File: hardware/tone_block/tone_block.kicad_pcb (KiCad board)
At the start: 2 copper layers, 48.1 x 18 mm, 18 parts, among them J1 I/O, Q1 RS32716R

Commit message: Tone block updated from comments
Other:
- board text added: "IN"
- board text added: "OUT"
- board text removed: "In"
- board text removed: "Mix"

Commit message: v1.01
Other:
- board text added: "Tone Block v1.01"

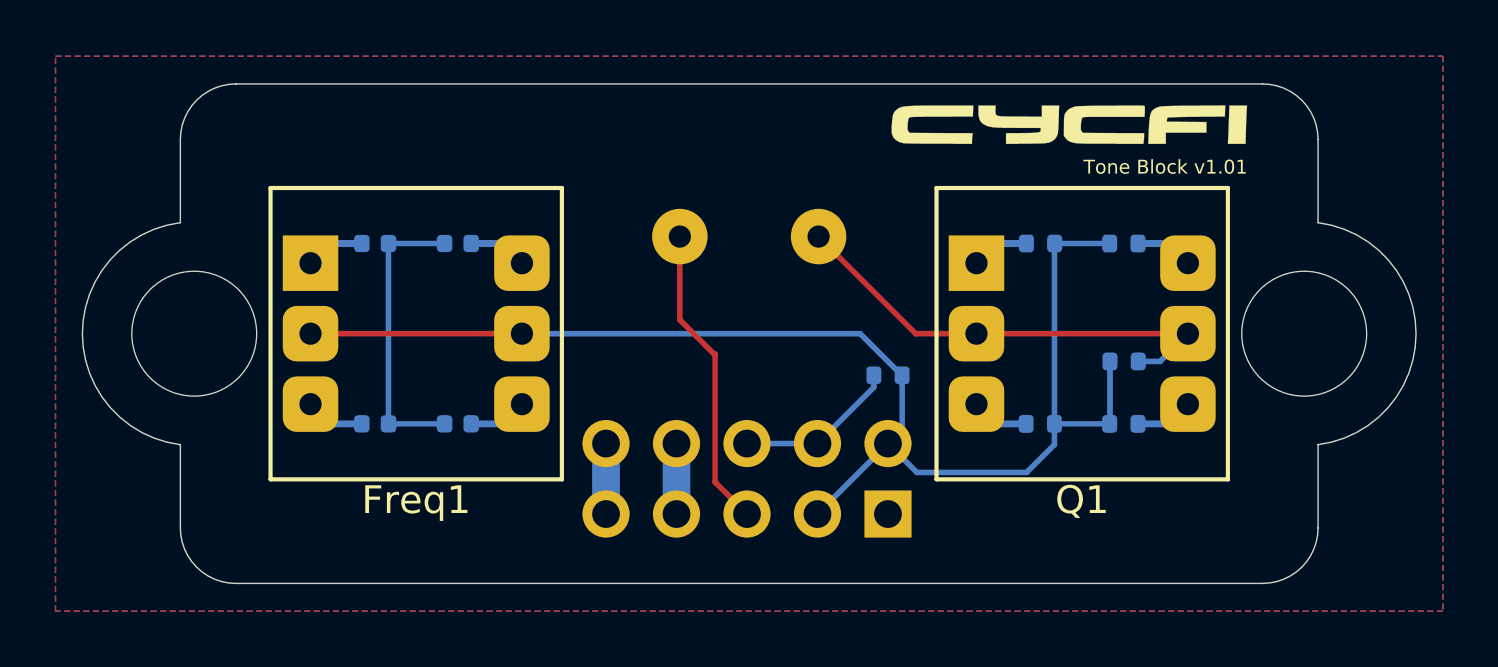
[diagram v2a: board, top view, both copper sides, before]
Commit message: Upgrade to kicad 6
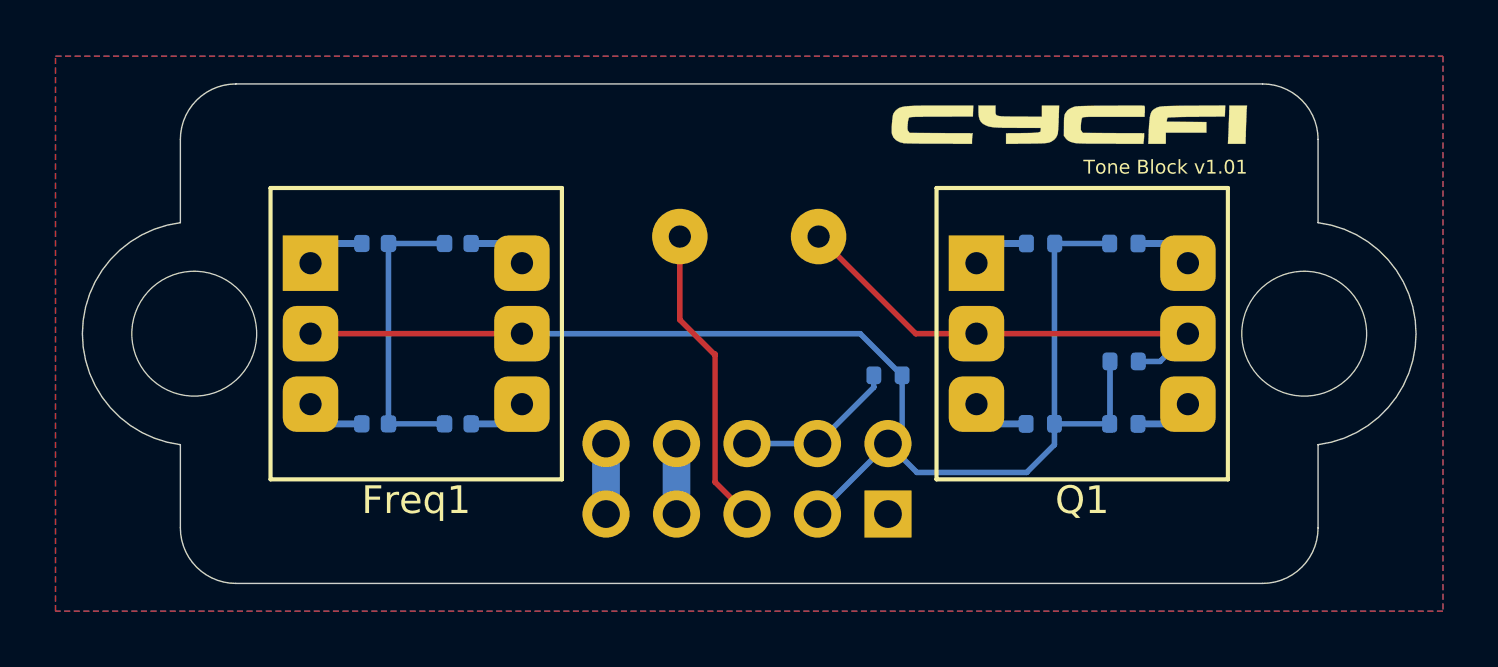
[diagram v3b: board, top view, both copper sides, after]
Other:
- net class Default removed

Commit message: Merge branch 'tone_block_v2' into devel
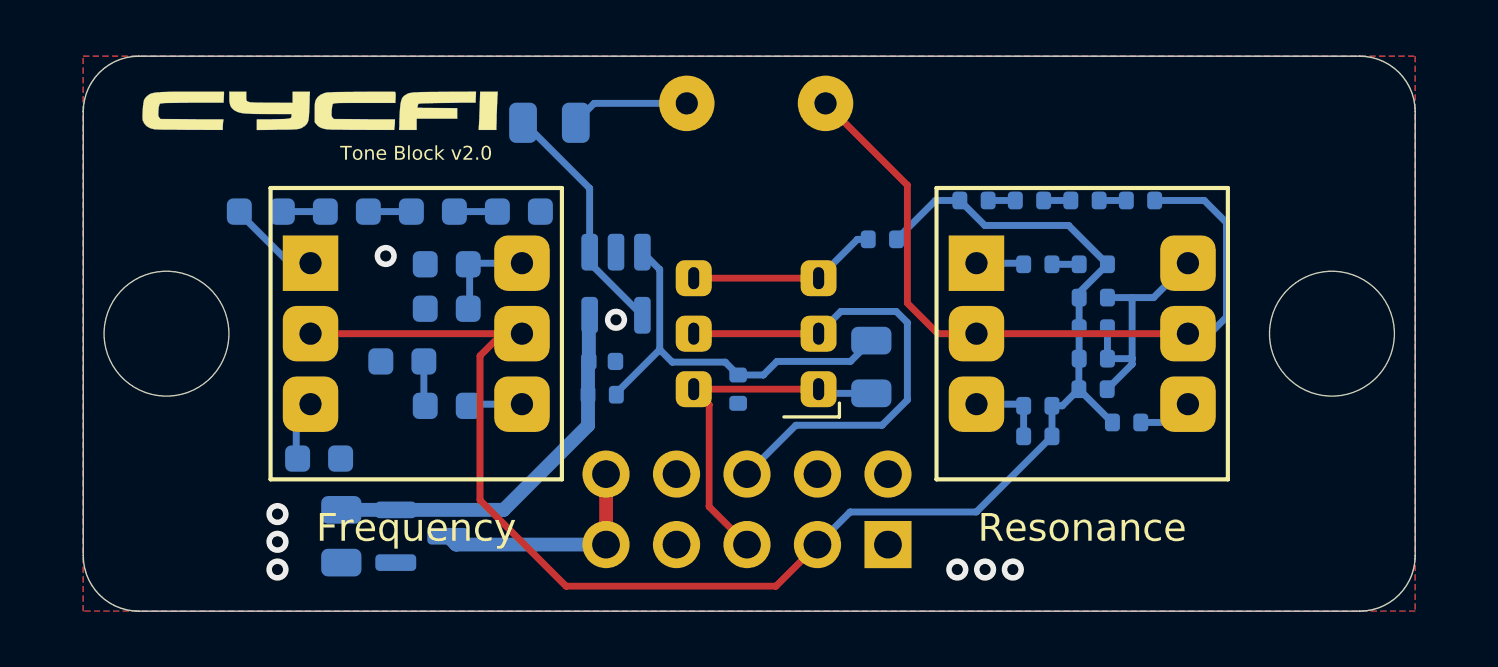
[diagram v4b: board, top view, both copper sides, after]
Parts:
- added C10: 47nF, Capacitor_SMD:C_0603_1608Metric, B.Cu at (190.5, 106.6)
- added C11: 47nF, Capacitor_SMD:C_0603_1608Metric, B.Cu at (192.5, 112.0)
- added C12: 47nF, Capacitor_SMD:C_0603_1608Metric, B.Cu at (193.6, 106.6)
- added C13: 47nF, Capacitor_SMD:C_0603_1608Metric, B.Cu at (196.7, 106.6)
- added C5: 47nF, Capacitor_SMD:C_0603_1608Metric, B.Cu at (187.4, 106.6)
- added C6: 47nF, Capacitor_SMD:C_0603_1608Metric, B.Cu at (194.1, 113.6)
- added C7: 47nF, Capacitor_SMD:C_0603_1608Metric, B.Cu at (189.5, 115.5)
- added C8: 47nF, Capacitor_SMD:C_0603_1608Metric, B.Cu at (194.1, 108.5)
- added C9: 47nF, Capacitor_SMD:C_0603_1608Metric, B.Cu at (194.1, 110.1)
- added Q2: LBSS84LT1G, Package_TO_SOT_SMD:SOT-23, B.Cu at (193.2, 118.3)
- added R10: 330, Resistor_SMD:R_0402_1005Metric, B.Cu at (218.6, 114.2)
- added R11: 330, Resistor_SMD:R_0402_1005Metric, B.Cu at (215.4, 113.6)
- added R12: 330, Resistor_SMD:R_0402_1005Metric, B.Cu at (215.4, 114.7)
- added R13: 330, Resistor_SMD:R_0402_1005Metric, B.Cu at (217.4, 109.7)
- added R14: 330, Resistor_SMD:R_0402_1005Metric, B.Cu at (217.4, 110.8)
- added R15: 330, Resistor_SMD:R_0402_1005Metric, B.Cu at (217.4, 111.9)
- added R16: 330, Resistor_SMD:R_0402_1005Metric, B.Cu at (217.4, 113.0)
- added R7: 330, Resistor_SMD:R_0402_1005Metric, B.Cu at (217.4, 108.5)
- added R8: 4.7k, Resistor_SMD:R_0402_1005Metric, B.Cu at (209.8, 107.6)
- added R9: 330, Resistor_SMD:R_0402_1005Metric, B.Cu at (215.4, 108.5)
- added SW1: DPDT, cycfi_library:PS5801, F.Cu at (207.5, 113.0)
- added U1: TLV170IDBVR, Package_TO_SOT_SMD:SOT-23-5, B.Cu at (200.2, 109.2)
- C1: value 12nF -> 4.7uF; footprint Capacitor_SMD:C_0402_1005Metric -> Capacitor_SMD:C_0805_2012Metric
- C2: value 27nF -> 0.1uF
- C3: value 47nF -> 10uF; footprint Capacitor_SMD:C_0402_1005Metric -> Capacitor_SMD:C_0805_2012Metric
- C4: value 100nF -> 10uF; footprint Capacitor_SMD:C_0402_1005Metric -> Capacitor_SMD:C_0805_2012Metric
- J1: footprint cycfi_library:pin_header_2x05_P2.54mm_vertical -> cycfi_library:pin_header_2x5_P2.54mm_vertical
- R1: value 1.33k -> 100k
- R2: value 665 -> 100k
- R4: value 165 -> 330
- R5: value 82.5 -> 330
- R6: value 4.7k -> 330
- moved G*** 27.5 mm to (220.5, 103.0)
- moved G*** 27.0 mm to (189.5, 103.0)
- moved R1 18.8 mm to (199.7, 113.2)
- moved C3 18.0 mm to (209.4, 112.2), turned to -90 degrees
- moved R2 12.1 mm to (204.6, 113.0), turned to -90 degrees
- moved R6 11.1 mm to (219.1, 106.2), turned to 0 degrees
- moved C1 10.6 mm to (190.3, 118.3), turned to 90 degrees
- moved R3 9.69 mm to (213.1, 106.2)
- moved R4 8.06 mm to (215.1, 106.2), turned to 0 degrees
- moved C2 5.67 mm to (199.7, 112.0), turned to 180 degrees
- moved C4 5.46 mm to (197.8, 103.4), turned to 180 degrees
- moved L1 4.81 mm to (205.2, 102.7)
- moved R5 2.09 mm to (217.1, 106.2)
- moved J1 1.10 mm to (210.0, 118.6)
- moved H1 1.00 mm to (184.0, 111.0)
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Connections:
- C1 pad 1: Net-(C1-Pad1) -> GND
- C1 pad 2: GND -> vcc
- C2 pad 2: Net-(C2-Pad2) -> vcc
- C3 pad 1: GND -> /op+
- C3 pad 2: Net-(C3-Pad2) -> in
- C4 pad 1: GND -> reso_in
- C4 pad 2: Net-(C4-Pad2) -> /op_out
- Freq1 pad 1: Net-(C1-Pad1) -> Net-(C5-Pad1)
- Freq1 pad 2: Net-(C2-Pad2) -> Net-(C6-Pad1)
- Freq1 pad 4: Net-(C3-Pad2) -> Net-(C7-Pad1)
- Freq1 pad 8: Net-(C4-Pad2) -> Net-(C8-Pad1)
- J1 pad 10: ext_cap -> unconnected-(J1-Pad10)
- J1 pad 5: vcc -> v+
- J1 pad 6: vcc -> v+
- J1 pad 8: mix -> out
- J1 pad 9: mix -> unconnected-(J1-Pad9)
- L1 pad 1: in -> reso_in
- R1 pad 1: ext_cap -> vcc
- R1 pad 2: Net-(L1-Pad2) -> /op+
- R2 pad 1: ext_cap -> /op+
- R2 pad 2: Net-(Q1-Pad1) -> GND
- R3 pad 2: Net-(Q1-Pad2) -> Net-(R3-Pad2)
- R4 pad 1: ext_cap -> Net-(R3-Pad2)
- R4 pad 2: Net-(Q1-Pad4) -> Net-(R4-Pad2)
- R5 pad 1: ext_cap -> Net-(R4-Pad2)
- R5 pad 2: Net-(Q1-Pad8) -> Net-(R5-Pad2)
- R6 pad 1: ext_cap -> Net-(R5-Pad2)
- R6 pad 2: mix -> Net-(L1-Pad2)
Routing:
- net out: track 0.00 -> 17.9 mm
- net /op+: track 0.00 -> 14.6 mm
- net GND: track 13.1 -> 0.00 mm, vias 0 -> 8
- net vcc: track 2.54 -> 14.1 mm
- net Net-(L1-Pad2): track 17.5 -> 26.9 mm
- net v+: track 0.00 -> 8.37 mm
- net /op_out: track 0.00 -> 8.32 mm
- net ext_cap: track 48.7 -> 56.9 mm
- net reso_out: track 0.00 -> 6.87 mm
- net Net-(Q1-Pad8): track 2.31 -> 9.08 mm
- net mix: track 5.84 -> 0.00 mm
- net reso_in: track 0.00 -> 4.33 mm
- net Net-(C8-Pad1): track 0.00 -> 3.50 mm
- net Net-(C5-Pad1): track 0.00 -> 3.39 mm
- net Net-(C7-Pad1): track 0.00 -> 2.88 mm
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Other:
- board size 48.1 x 18 mm -> 48 x 20 mm
- board text added: "Frequency"
- board text added: "Resonance"
- board text added: "Tone Block v2.0"
- board text removed: "GND"
- board text removed: "Mix Shunt"
- board text removed: "Tone Block v1.0"
- board text removed: "Tone Block v1.01"
- board text removed: "VCC"

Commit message: Simplified connections (simple IN / OUT, no extra fluff)
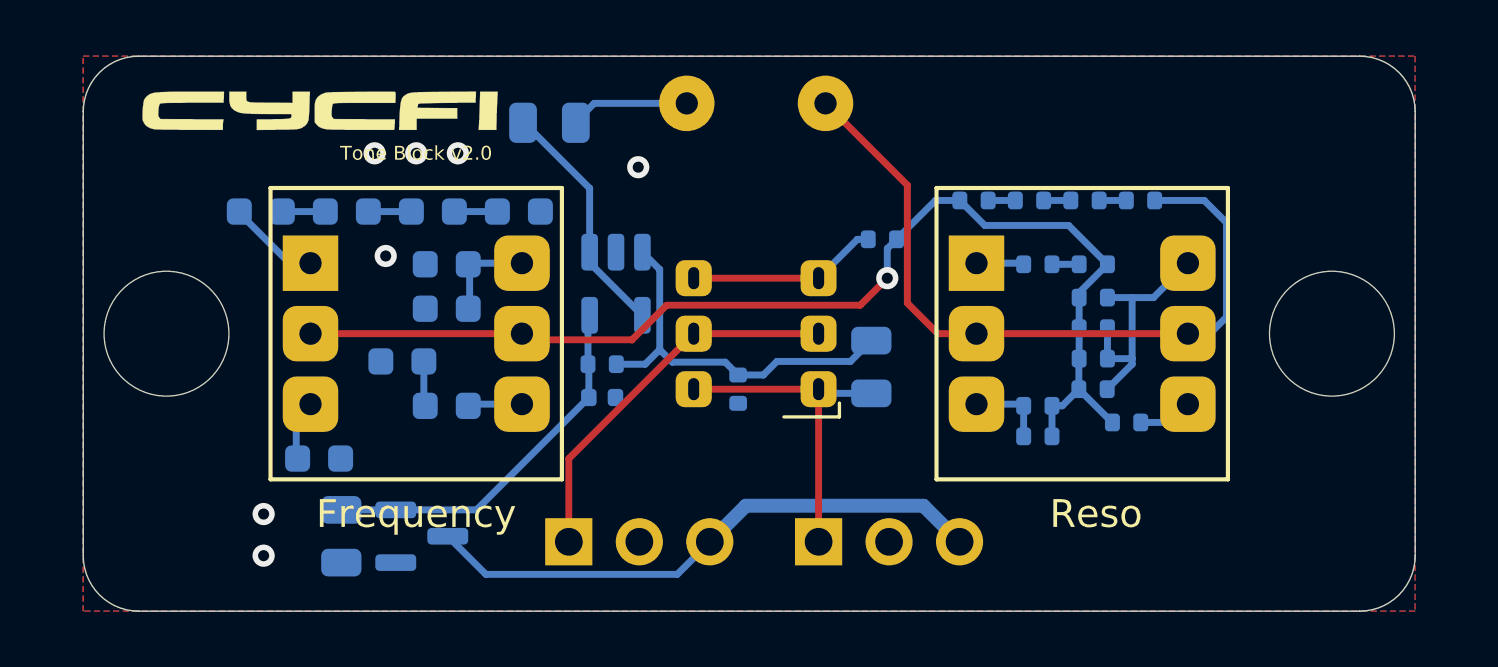
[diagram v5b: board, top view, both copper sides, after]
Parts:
- added J2: conn_1x3, Connector_PinHeader_2.54mm:PinHeader_1x03_P2.54mm_Vertical, B.Cu at (198.5, 118.5)
- C2: value 0.1uF -> 100nF
- J1: value I/O -> conn_1x3; footprint cycfi_library:pin_header_2x5_P2.54mm_vertical -> Connector_PinHeader_2.54mm:PinHeader_1x03_P2.54mm_Vertical
- moved J1 2.50 mm to (207.5, 118.5), turned to -90 degrees
- moved C2 1.30 mm to (199.7, 113.3)
- moved R1 1.10 mm to (199.7, 112.1)
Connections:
- Freq1 pad C: ext_cap -> Net-(Freq1-PadC)
- J1 pad 1: GND -> in
- J1 pad 2: ext_cap -> GND
- J1 pad 3: in -> v+
- R10 pad 1: ext_cap -> Net-(Freq1-PadC)
- R11 pad 1: ext_cap -> Net-(Freq1-PadC)
- R12 pad 1: ext_cap -> Net-(Freq1-PadC)
- R13 pad 1: ext_cap -> Net-(Freq1-PadC)
- R14 pad 1: ext_cap -> Net-(Freq1-PadC)
- R15 pad 1: ext_cap -> Net-(Freq1-PadC)
- R16 pad 1: ext_cap -> Net-(Freq1-PadC)
- R3 pad 1: ext_cap -> Net-(Freq1-PadC)
- R7 pad 1: ext_cap -> Net-(Freq1-PadC)
- R8 pad 1: ext_cap -> Net-(Freq1-PadC)
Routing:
- net ext_cap: track 56.9 -> 0.00 mm
- net Net-(Freq1-PadC): track 0.00 -> 41.4 mm, vias 0 -> 1
- net v+: track 8.37 -> 20.6 mm
- net out: track 17.9 -> 13.9 mm
- net in: track 12.6 -> 11.8 mm
- net vcc: track 14.1 -> 13.6 mm
- net GND: vias 8 -> 7
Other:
- board text added: "GND"
- board text added: "Reso"
- board text added: "V+"
- board text removed: "Ext Cap"
- board text removed: "Resonance"

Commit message: Updated layout
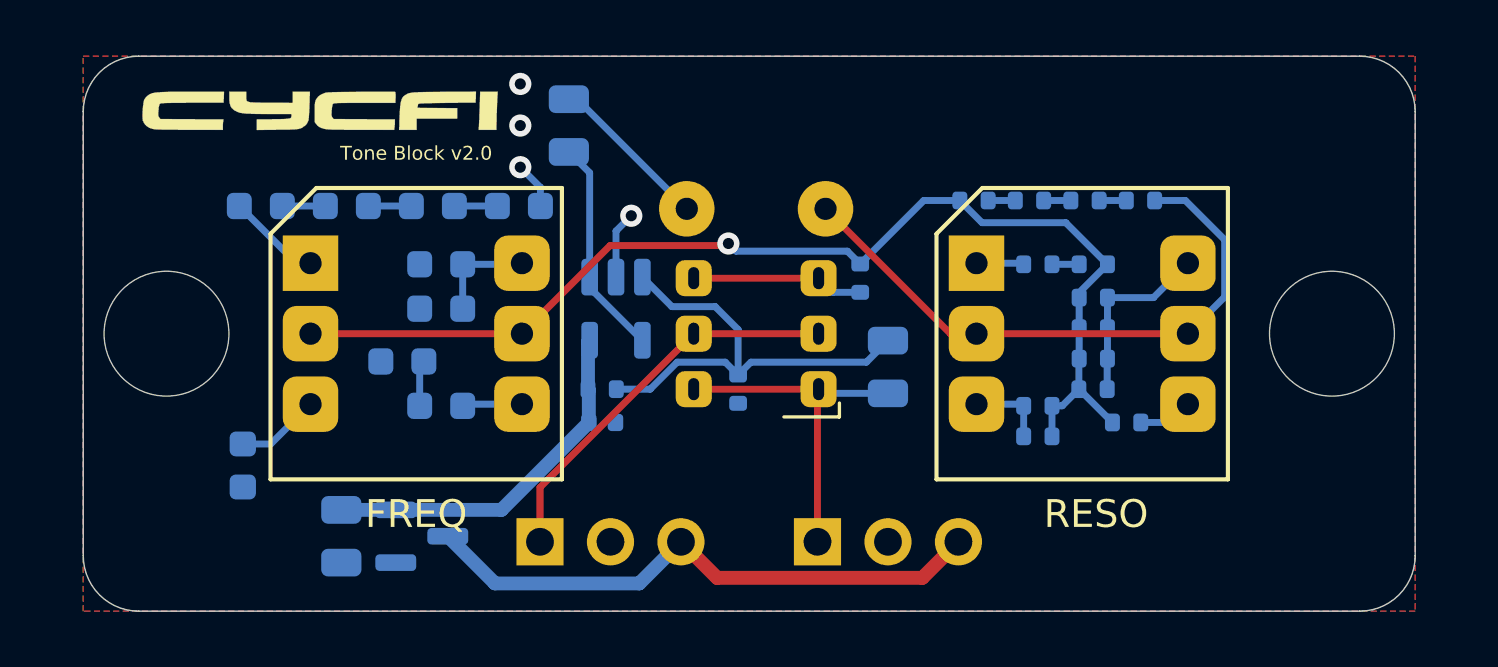
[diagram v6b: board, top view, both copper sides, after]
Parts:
- moved L1 3.80 mm to (205.2, 106.5)
- moved C7 2.76 mm to (186.8, 115.8), turned to -90 degrees
- moved J1 2.50 mm to (210.0, 118.5)
- moved R8 1.61 mm to (209.0, 109.0), turned to -90 degrees
- moved J2 1.50 mm to (200.0, 118.5)
- moved C2 0.90 mm to (199.7, 114.2)
- moved R1 0.90 mm to (199.7, 113.0)
- moved U1 0.90 mm to (200.2, 110.1)
- moved C4 0.71 mm to (198.5, 103.5), turned to -90 degrees
- moved C3 0.60 mm to (210.0, 112.2)
- moved C10 0.20 mm to (190.5, 106.4)
- moved C12 0.20 mm to (193.6, 106.4)
- moved C13 0.20 mm to (196.7, 106.4)
- moved C5 0.20 mm to (187.4, 106.4)
- moved C6 0.20 mm to (193.9, 113.6)
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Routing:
- net Net-(L1-Pad2): track 26.9 -> 22.0 mm
- net GND: track 0.00 -> 4.14 mm, vias 7 -> 4
- net /op+: track 14.1 -> 16.8 mm
- net Net-(Q1-Pad8): track 9.08 -> 6.72 mm
- net reso_in: track 4.33 -> 5.89 mm
- net in: track 11.8 -> 12.6 mm
- net /op_out: track 8.71 -> 7.89 mm
- net reso_out: track 6.87 -> 6.21 mm
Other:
- board text added: "FREQ"
- board text added: "RESO"
- board text removed: "Frequency"
- board text removed: "Reso"
